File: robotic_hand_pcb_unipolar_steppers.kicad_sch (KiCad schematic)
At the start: 15 parts, among them J13 JST 1x5 Male, J14 JST 1x5 Male, J15 JST 1x5 Male, J16 JST 1x5 Male, J17 JST 1x5 Male, U14 ULN2003ADR, U15 ULN2003ADR, U16 ULN2003ADR, U17 ULN2003ADR, U18 ULN2003ADR

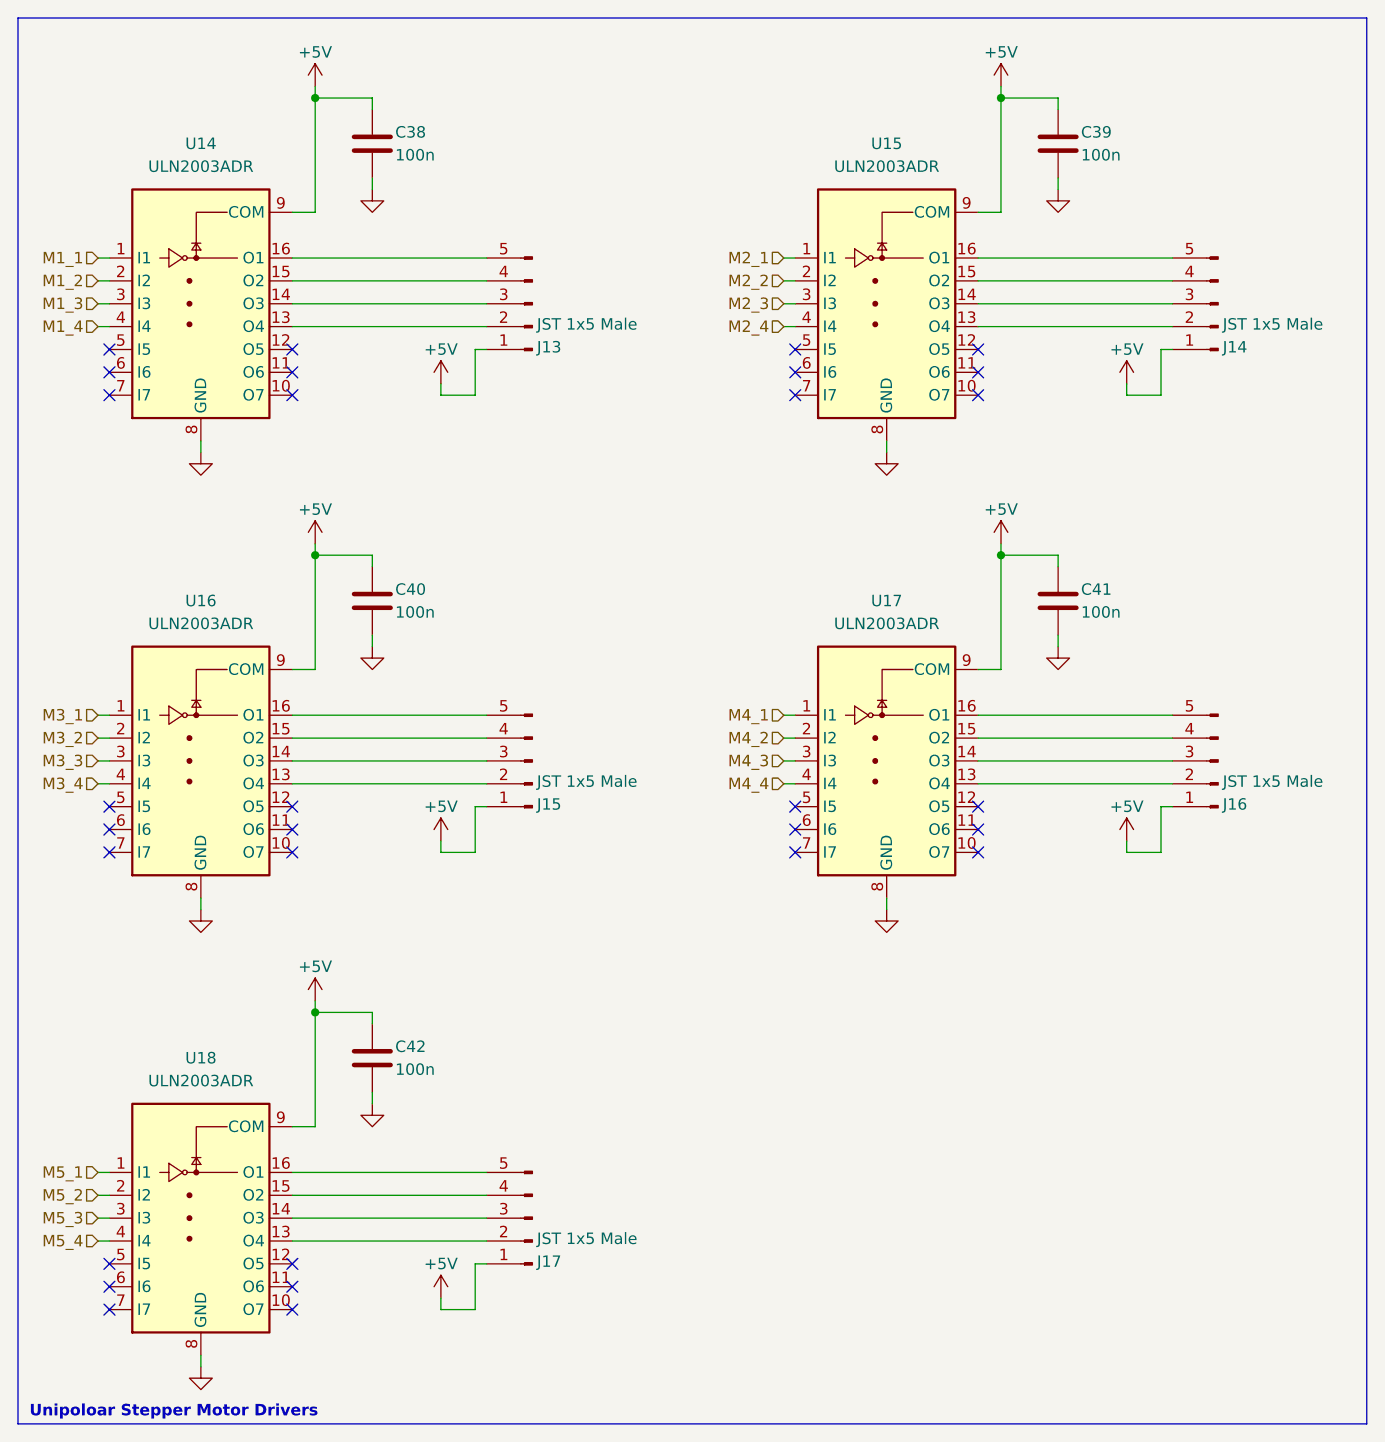
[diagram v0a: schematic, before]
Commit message: Route power, add major cleanup
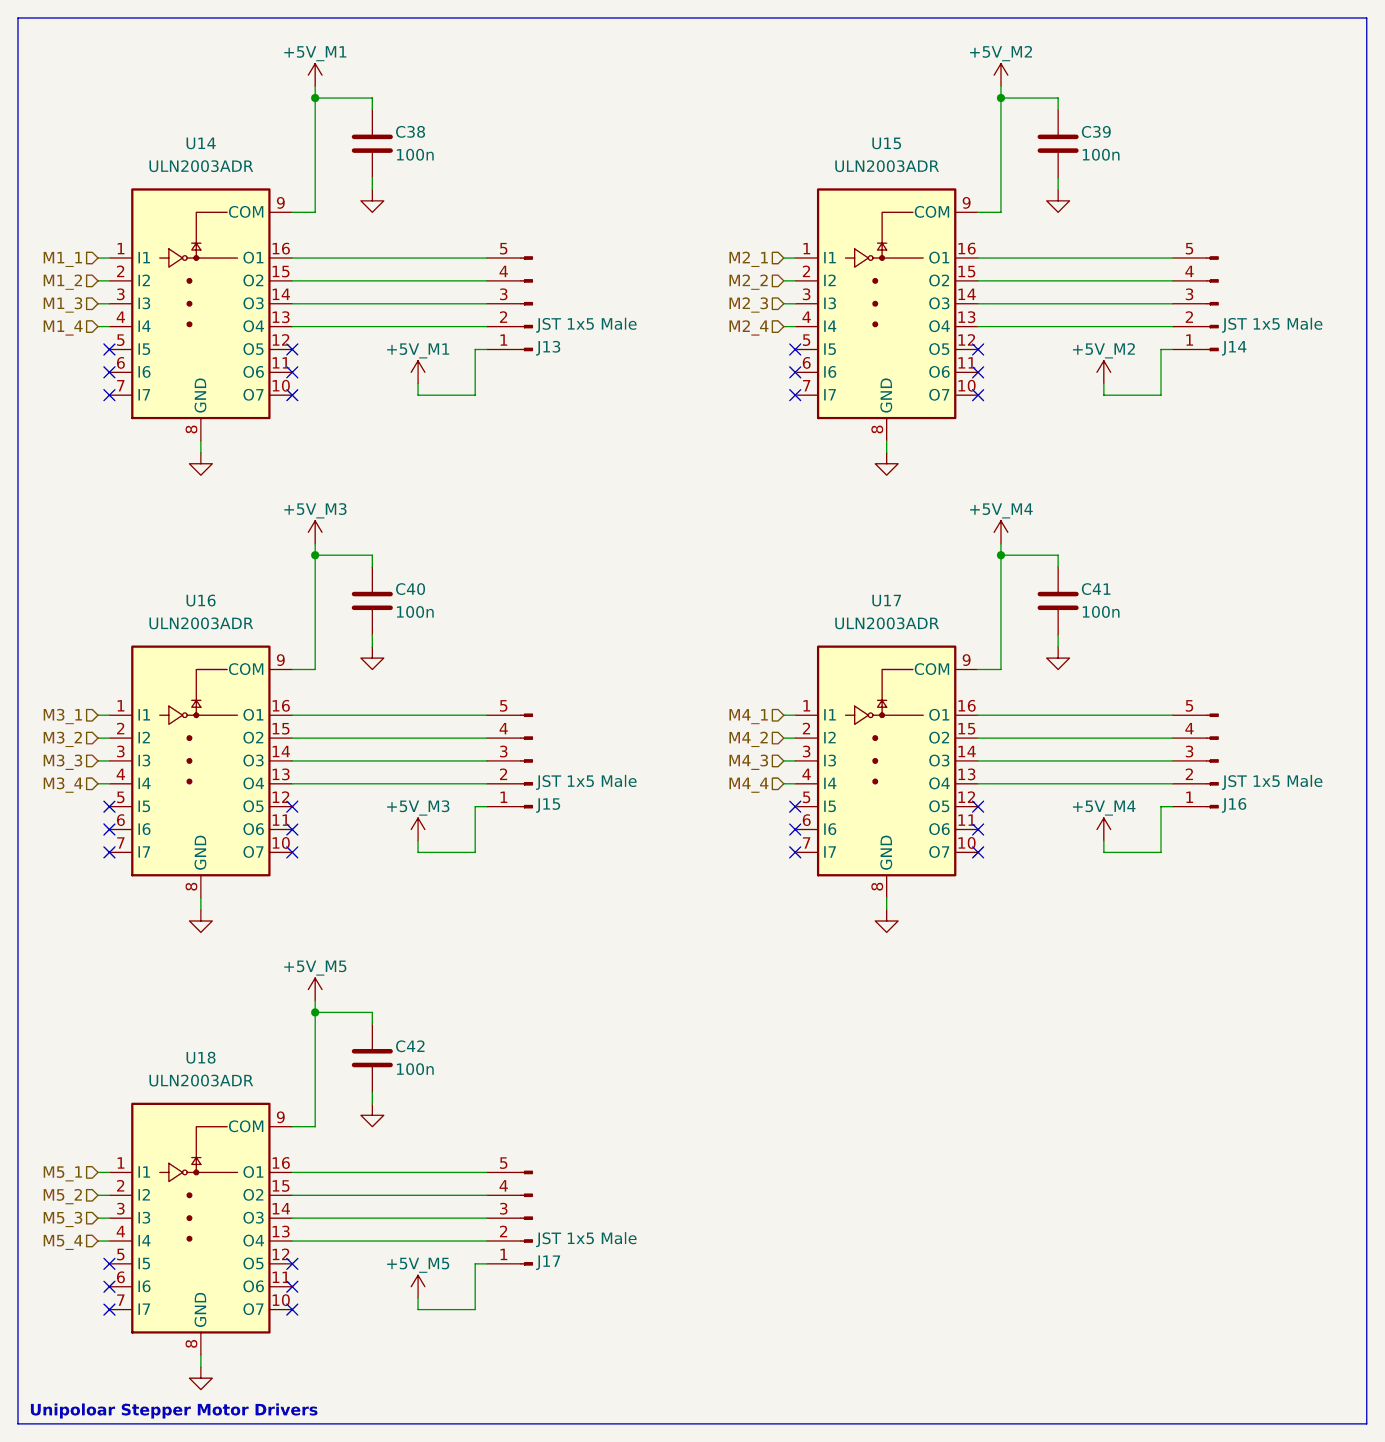
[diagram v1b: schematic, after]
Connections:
- removed net +5V: C38.1, C39.1, C40.1, C41.1, C42.1, J13.1 (Pin_1), J14.1 (Pin_1), J15.1 (Pin_1), J16.1 (Pin_1), J17.1 (Pin_1), U14.9 (COM), U15.9 (COM), U16.9 (COM), U17.9 (COM), U18.9 (COM)
- new net +5V_M1: C38.1, J13.1 (Pin_1), U14.9 (COM)
- new net +5V_M2: C39.1, J14.1 (Pin_1), U15.9 (COM)
- new net +5V_M3: C40.1, J15.1 (Pin_1), U16.9 (COM)
- new net +5V_M4: C41.1, J16.1 (Pin_1), U17.9 (COM)
- new net +5V_M5: C42.1, J17.1 (Pin_1), U18.9 (COM)

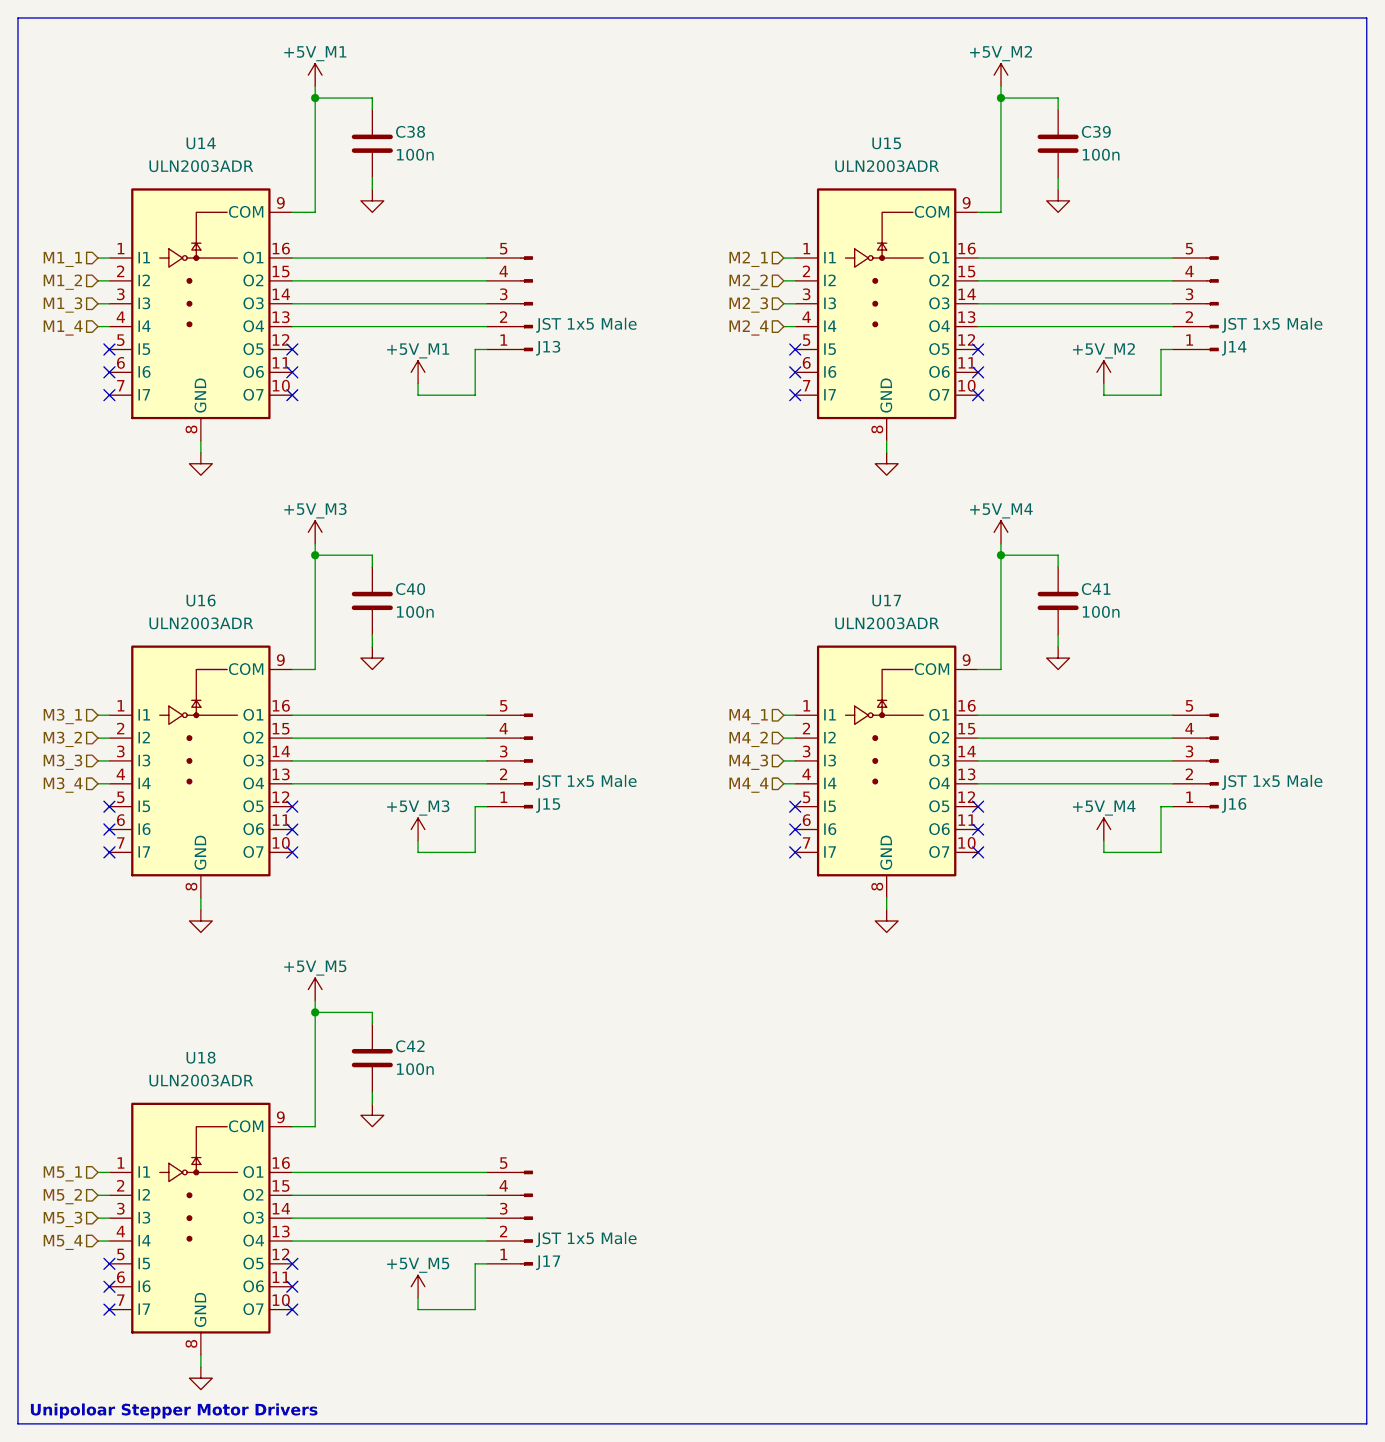
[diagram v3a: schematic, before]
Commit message: Initial full PCB design, pass DRC
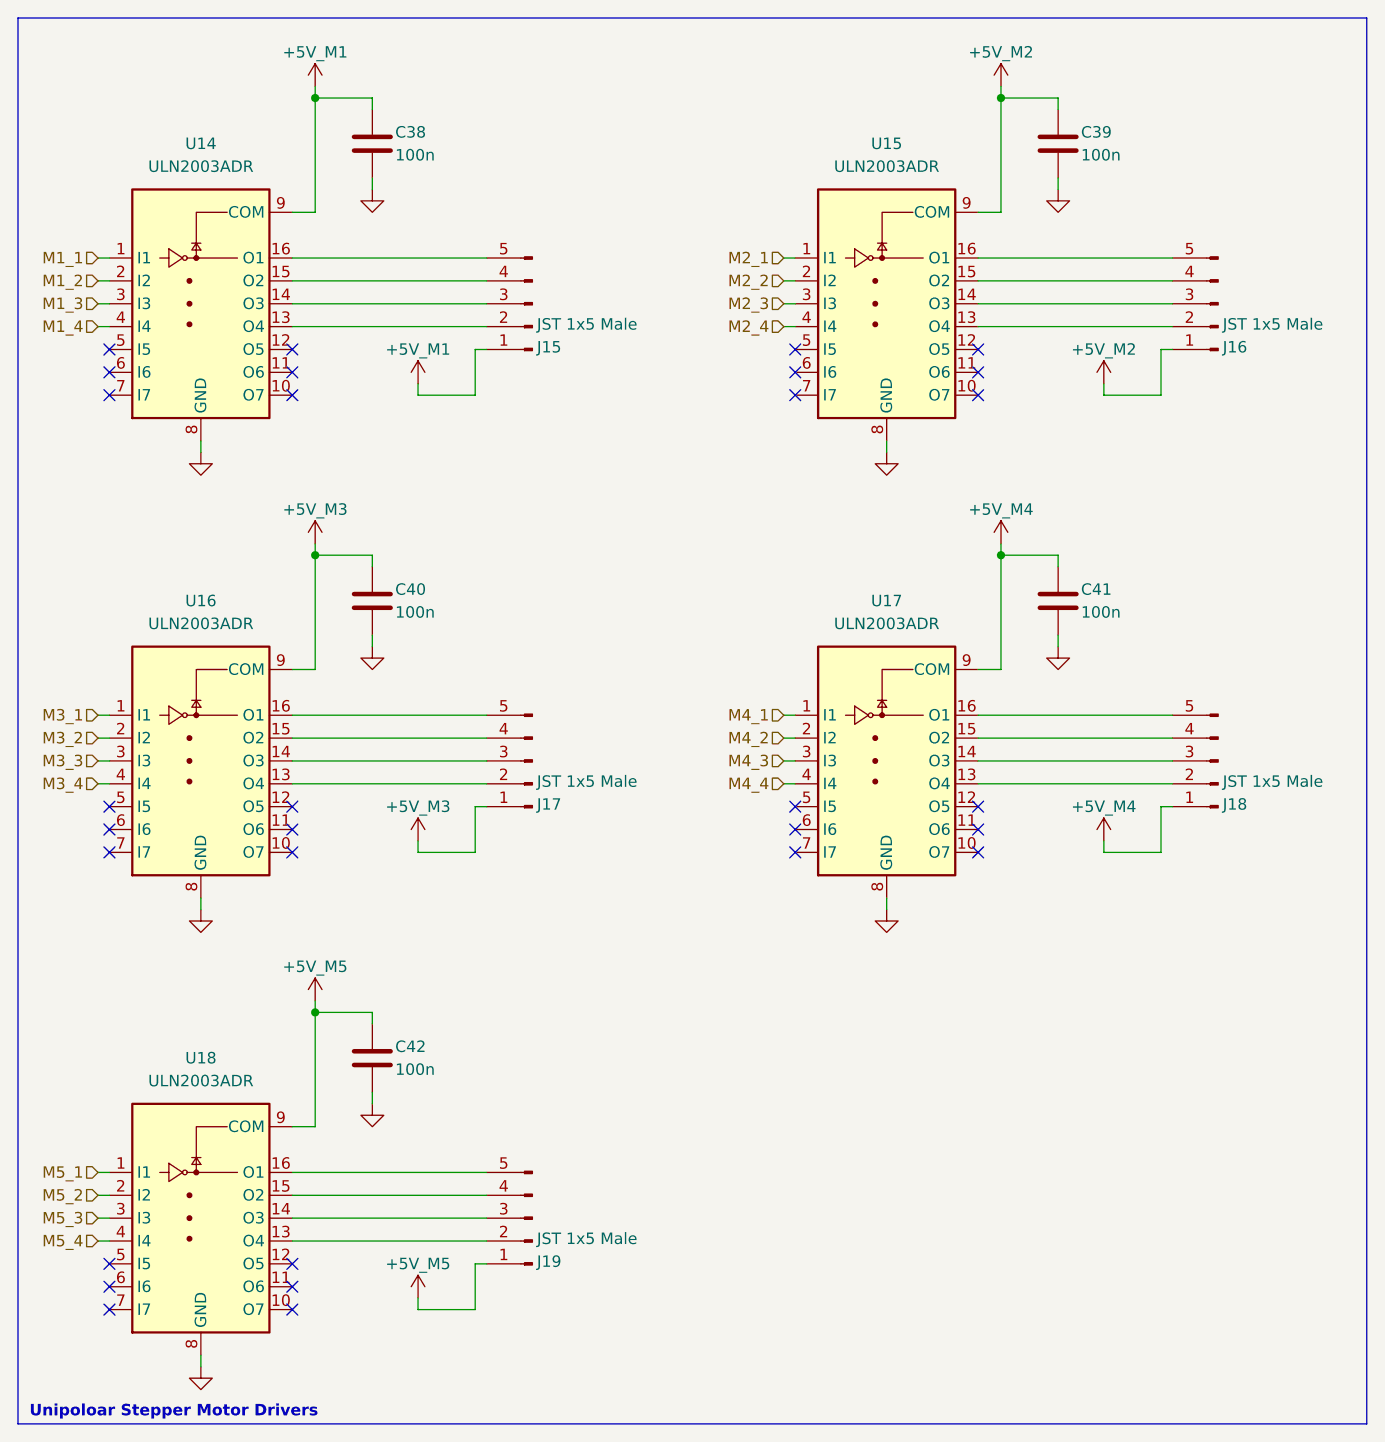
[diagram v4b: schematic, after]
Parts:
- renumbered J13 to J15, J14 to J16, J15 to J17, J16 to J18, J17 to J19
